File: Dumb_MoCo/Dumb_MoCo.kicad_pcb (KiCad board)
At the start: 2 copper layers, 32.7 x 55.3 mm, 18 parts, among them U1 VNH7070AS

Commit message: Rearranged res, added silkscreenssss
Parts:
- added G***: LOGO, MRDT_Silkscreens:0_MRDT_Logo_10mm, F.Cu at (133.9, 74.2)
- added G***: LOGO, Signatures:WillGroveSignatureMedium, F.Cu at (121.9, 83.9)
- added G***: LOGO, Signatures:WillGroveFaceTiny, B.Cu at (134.7, 95.2)
- moved R2 3.31 mm to (144.7, 104.4)
- moved C4 3.16 mm to (145.5, 107.3), turned to 180 degrees
- moved R6 1.29 mm to (148.7, 104.4)
- moved R1 0.79 mm to (146.7, 104.4)
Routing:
- net CS: track 19.0 -> 10.3 mm
- net Net-(U1-SEL): track 19.4 -> 17.5 mm
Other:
- board text added: "12V"
- board text added: "Brushed Dumb MoCo, Rev1 Mars Rover Design Team Missouri S&T, 2025 Will Grove"
- board text added: "GND"
- board text added: "M+"
- board text added: "M-"

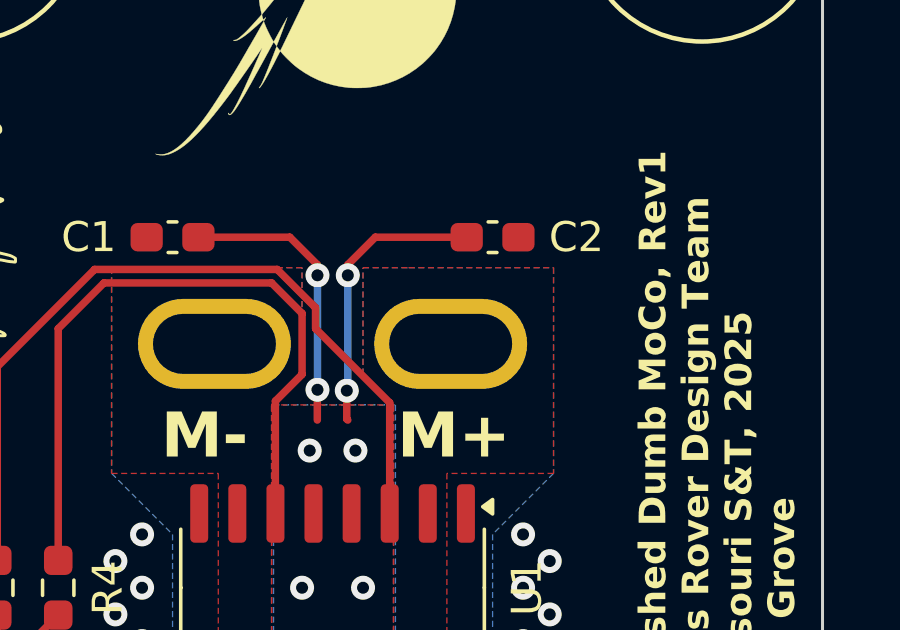
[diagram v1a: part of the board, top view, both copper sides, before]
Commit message: Removed C1
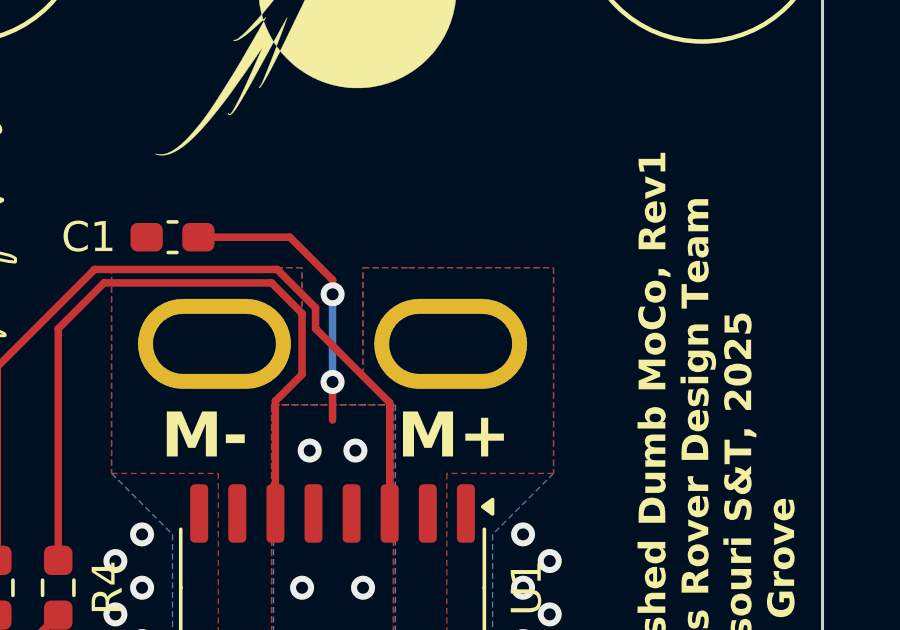
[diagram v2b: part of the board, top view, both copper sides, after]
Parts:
- removed C2: 0.1uF, Capacitor_SMD:C_0603_1608Metric_Pad1.08x0.95mm_HandSolder
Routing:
- net +12V: track 19.1 -> 9.74 mm, vias 9 -> 7

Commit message: Added Chamber Ult Silkscreen
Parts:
- removed the G*** at (134.7, 95.2)
- added G***: LOGO, Signatures:ChamberUlt, B.Cu at (134.7, 95.0)

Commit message: Started on layout
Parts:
- removed C1: 10uF, Capacitor_SMD:C_0603_1608Metric_Pad1.08x0.95mm_HandSolder
- removed G***: LOGO, MRDT_Silkscreens:0_MRDT_Logo_10mm
- removed G***: LOGO, Signatures:WillGroveSignatureMedium
- removed G***: LOGO, Signatures:ChamberUlt
- removed V1, V2, V3, V4: Via, MRDT_Drill_Holes:4_40_Hole
- added C2: 0.1uF, Capacitor_SMD:C_0603_1608Metric_Pad1.08x0.95mm_HandSolder, F.Cu at (94.2, 52.5)
- Conn1, Conn2: moved to F.Cu
- moved C4 73.3 mm to (94.2, 55.0), turned to 0 degrees
- moved R1 70.4 mm to (94.2, 57.5), turned to 0 degrees
- moved R2 67.1 mm to (94.2, 60.0), turned to 0 degrees
- moved R6 64.4 mm to (94.2, 70.0), turned to 0 degrees
- moved R5 49.2 mm to (94.2, 67.5), turned to 0 degrees
- moved C3 46.4 mm to (164.0, 80.9), turned to 0 degrees
- moved Conn3 45.3 mm to (148.6, 65.0), turned to 0 degrees
- moved R3 42.7 mm to (94.2, 62.5), turned to 0 degrees
- moved R4 42.4 mm to (94.2, 65.0), turned to 0 degrees
- moved U1 28.0 mm to (153.7, 73.0)
- moved Conn2 26.0 mm to (149.2, 80.1)
- moved Conn1 17.6 mm to (141.6, 72.4), turned to 0 degrees
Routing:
- net IN_A: track 34.4 -> 0.00 mm
- net IN_B: track 31.6 -> 0.00 mm
- net Net-(U1-IN_A): track 26.8 -> 0.00 mm
- net Net-(U1-IN_B): track 23.9 -> 0.00 mm
- net Net-(U1-PWM): track 18.9 -> 0.00 mm
- net Net-(U1-SEL): track 17.5 -> 0.00 mm
- net Net-(U1-CS): track 16.3 -> 0.00 mm
- net SEL: track 12.5 -> 0.00 mm
- net CS: track 10.3 -> 0.00 mm
- net PWM: track 9.90 -> 0.00 mm
- net +12V: track 9.74 -> 0.00 mm, vias 7 -> 0
- net GND: vias 10 -> 0
- net /M-: vias 1 -> 0
- net /M+: vias 1 -> 0
- removed copper zone on B.Cu, net +12V
- removed copper zone on B.Cu, net GND
- removed copper zone on F.Cu, net GND
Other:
- board size 32.7 x 55.3 mm -> 38.1 x 38.1 mm
- board text removed: "12V"
- board text removed: "Brushed Dumb MoCo, Rev1 Mars Rover Design Team Missouri S&T, 2025 Will Grove"
- board text removed: "GND"
- board text removed: "M+"
- board text removed: "M-"

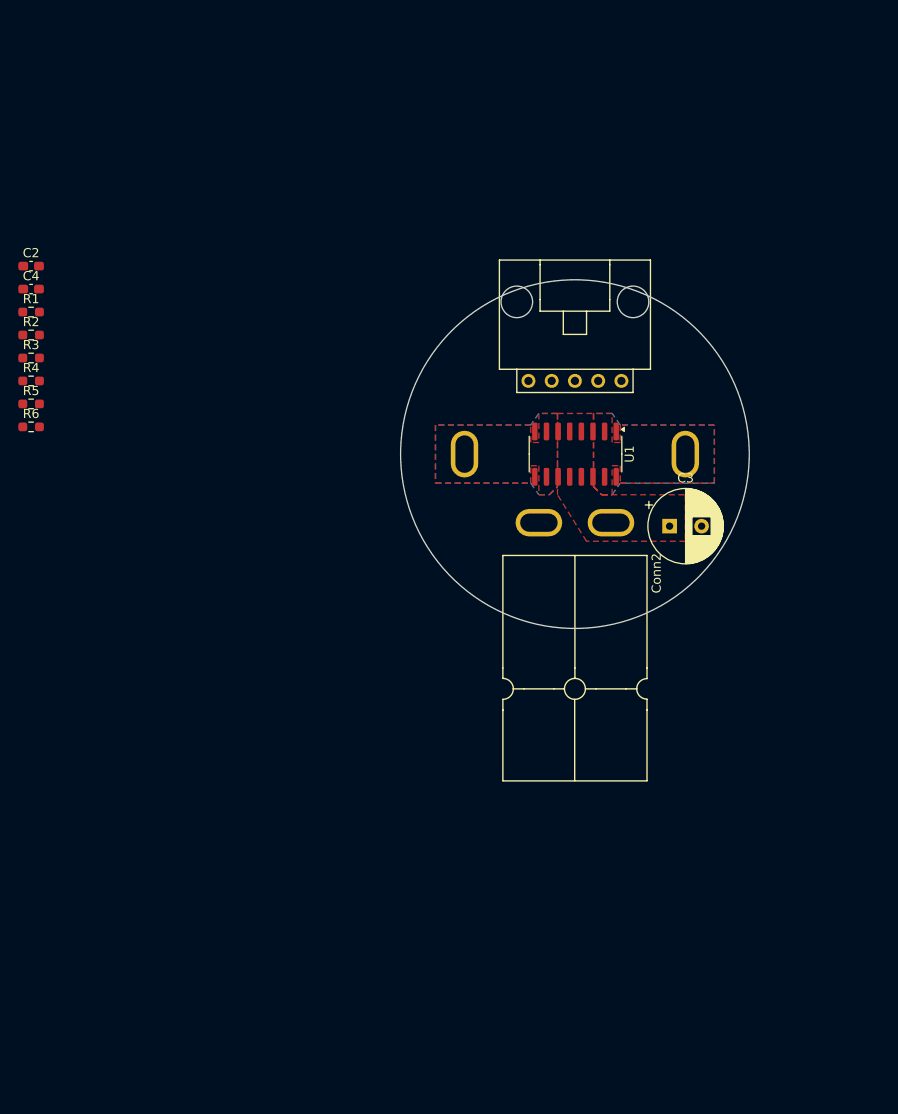
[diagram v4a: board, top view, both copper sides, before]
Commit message: Finished layout draft
made anderson and SL vertical
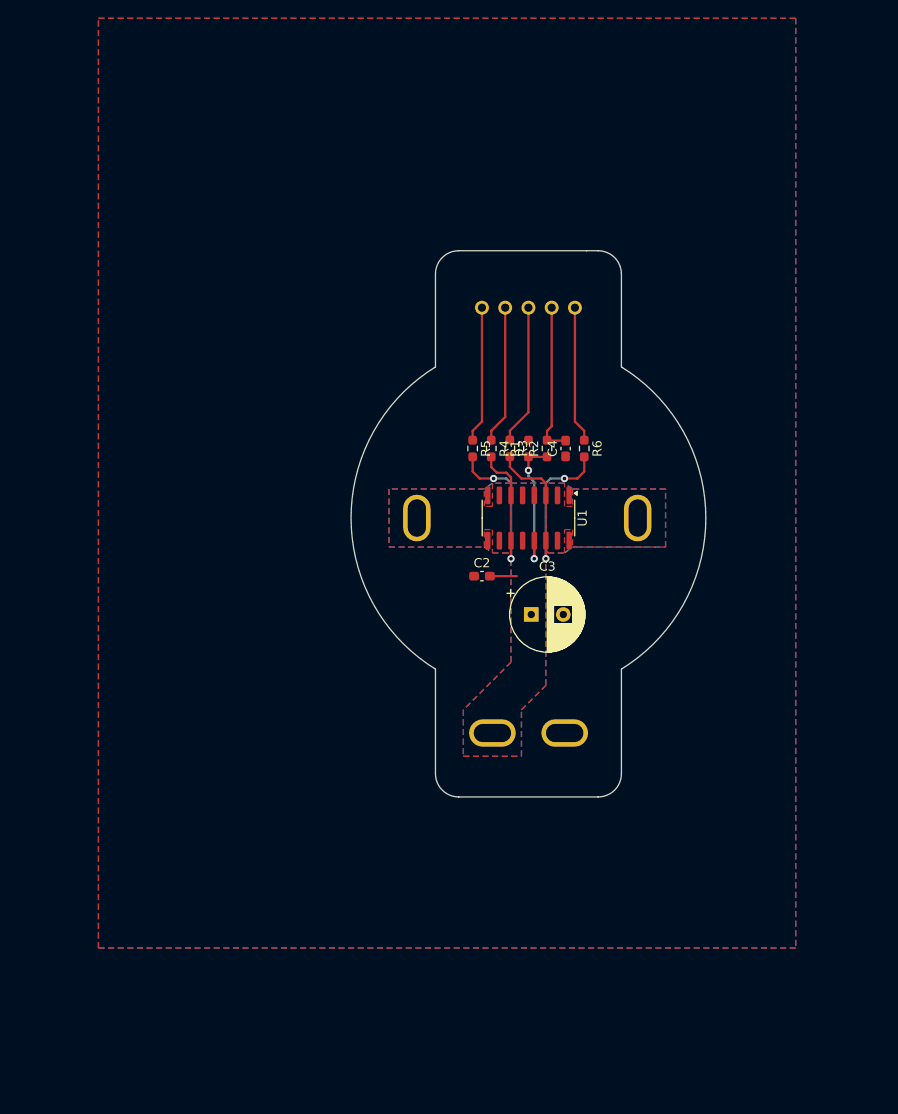
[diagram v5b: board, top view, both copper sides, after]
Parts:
- Conn2: footprint MRDT_Connectors:Square_Anderson_2_H_Side_By_Side -> MRDT_Connectors:Square_Anderson_2_V_Side_By_Side; moved to B.Cu
- Conn3: footprint MRDT_Connectors:MOLEX_SL_05_Horizontal -> MRDT_Connectors:MOLEX_SL_05_Vertical; moved to B.Cu
- moved C4 61.0 mm to (152.7, 72.4), turned to 90 degrees
- moved R6 60.5 mm to (154.7, 72.4), turned to -90 degrees
- moved C2 59.8 mm to (143.5, 86.4)
- moved R2 57.7 mm to (150.6, 72.4), turned to 90 degrees
- moved R1 56.4 mm to (148.6, 72.4), turned to 90 degrees
- moved R3 53.2 mm to (146.6, 72.4), turned to -90 degrees
- moved R4 50.8 mm to (144.5, 72.4), turned to -90 degrees
- moved R5 48.5 mm to (142.5, 72.4), turned to -90 degrees
- moved Conn2 23.2 mm to (148.5, 103.4), turned to 180 degrees
- moved C3 17.9 mm to (148.9, 90.6)
- moved Conn3 9.48 mm to (153.7, 57.0), turned to 180 degrees
- moved Conn1 9.23 mm to (136.4, 80.0)
- moved U1 8.68 mm to (148.6, 80.0)
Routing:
- net CS: track 0.00 -> 16.7 mm
- net Net-(U1-SEL): track 0.00 -> 16.5 mm, vias 0 -> 2
- net Net-(U1-PWM): track 0.00 -> 16.5 mm, vias 0 -> 2
- net Net-(U1-CS): track 0.00 -> 15.4 mm, vias 0 -> 2
- net IN_A: track 0.00 -> 15.3 mm
- net IN_B: track 0.00 -> 15.1 mm
- net SEL: track 0.00 -> 14.9 mm
- net PWM: track 0.00 -> 14.9 mm
- net Net-(U1-IN_A): track 0.00 -> 7.13 mm
- net Net-(U1-IN_B): track 0.00 -> 5.71 mm
- net +12V: track 0.00 -> 2.95 mm
- added copper zone on B.Cu, net +12V
- added copper zone on B.Cu, net GND
- added copper zone on F.Cu, net GND
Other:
- board size 38.1 x 38.1 mm -> 38.8 x 59.7 mm

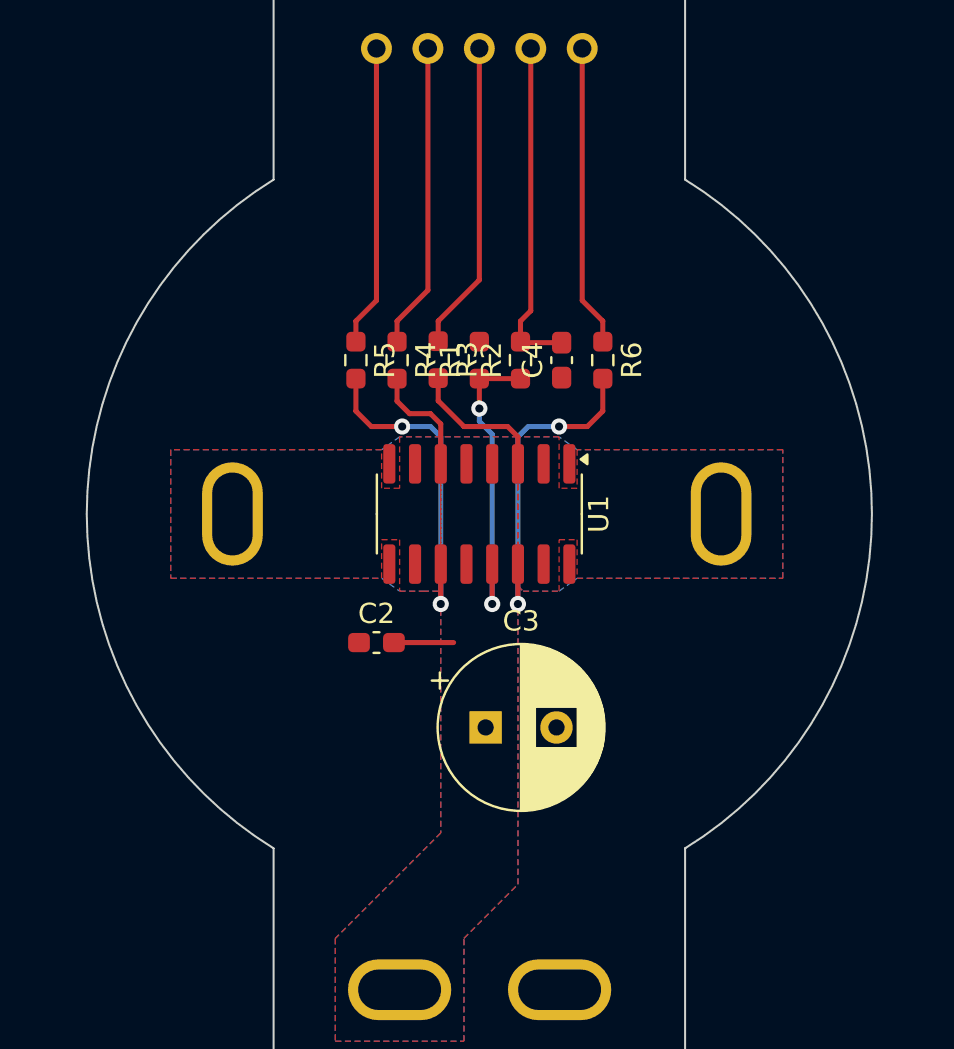
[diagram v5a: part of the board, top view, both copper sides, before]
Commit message: Updated silkscreen
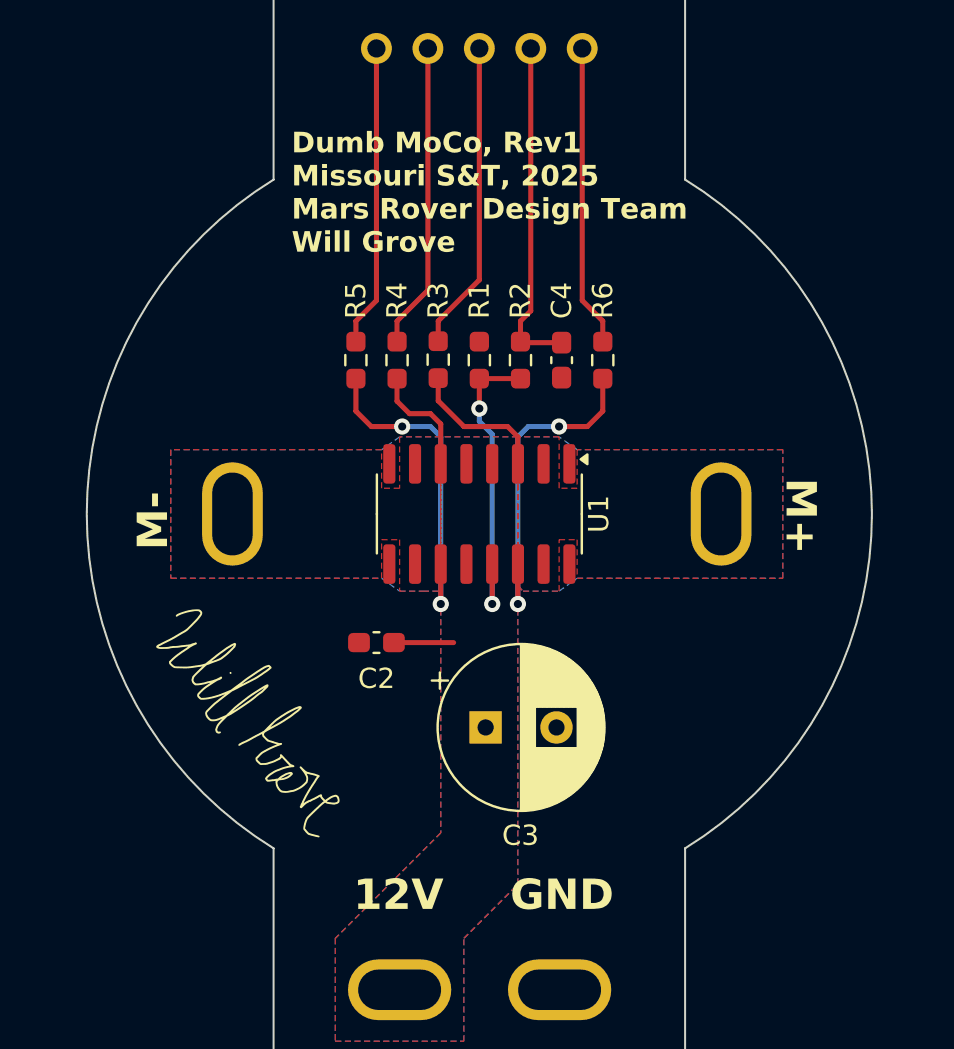
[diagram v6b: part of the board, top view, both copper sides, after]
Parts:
- added G***: LOGO, Signatures:WillGroveSignatureMedium, F.Cu at (137.5, 90.0)
- added G***: LOGO, Signatures:ChamberUlt, B.Cu at (148.5, 80.0)
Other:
- board text added: "12V"
- board text added: "Dumb MoCo, Rev1 Missouri S&T, 2025 Mars Rover Design Team Will Grove"
- board text added: "GND"
- board text added: "M+"
- board text added: "M-"

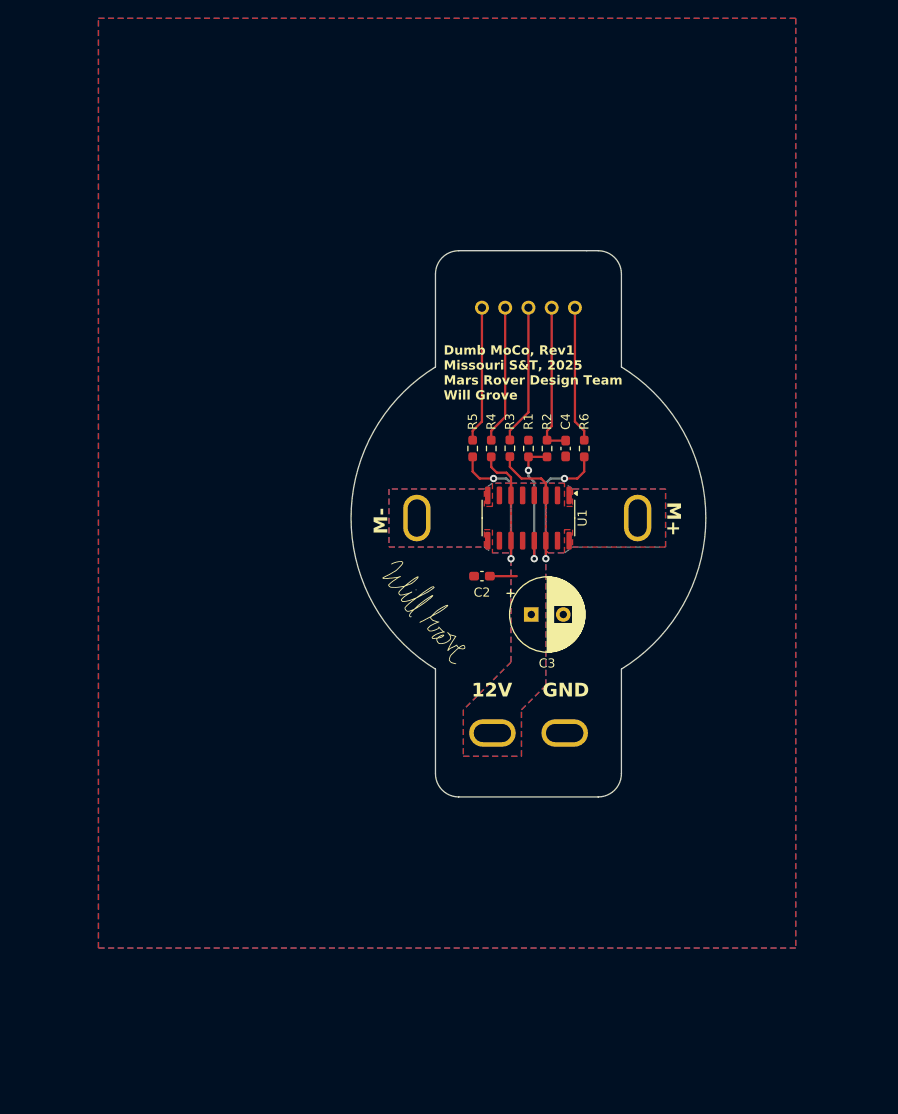
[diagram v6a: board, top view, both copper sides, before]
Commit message: Added vias and made 12V plane wider
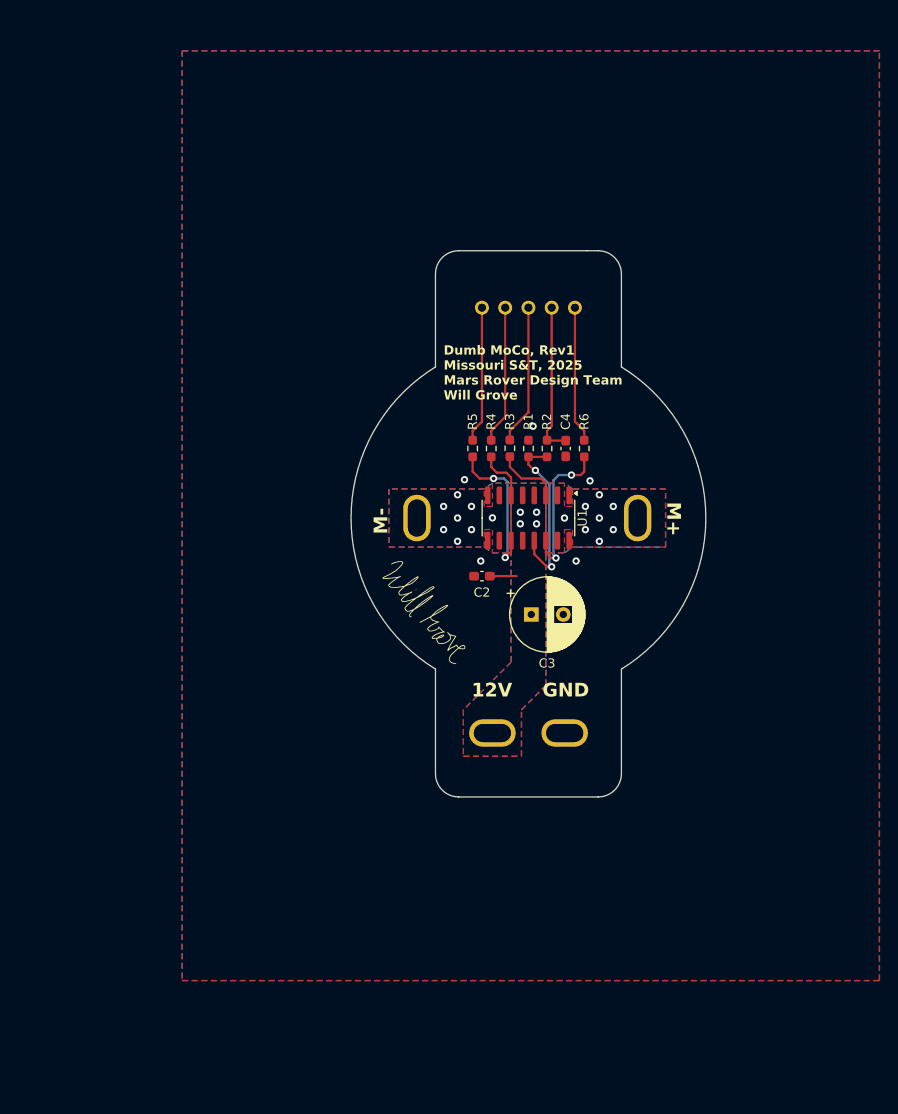
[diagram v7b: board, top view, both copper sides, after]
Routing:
- net Net-(U1-CS): track 15.4 -> 19.1 mm
- net GND: vias 0 -> 5
- net /M-: vias 0 -> 8
- net /M+: vias 0 -> 8
- net +12V: vias 0 -> 4

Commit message: more vias
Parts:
- added G***: LOGO, MRDT_Silkscreens:0_MRDT_Logo_7.5mm, F.Cu at (161.8, 87.4)
